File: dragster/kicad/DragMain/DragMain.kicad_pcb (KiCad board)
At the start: 2 copper layers, 56 x 100 mm, 23 parts, among them J1 Aux, J2 Servo 1, J3 Battery, J4 Motor L, J5 Motor R, J6 Sensors, J7 Motor L2, J8 Motor R2, U1 DFROBOT_HR8833, U2 TTGO_ESP32_TDisplay

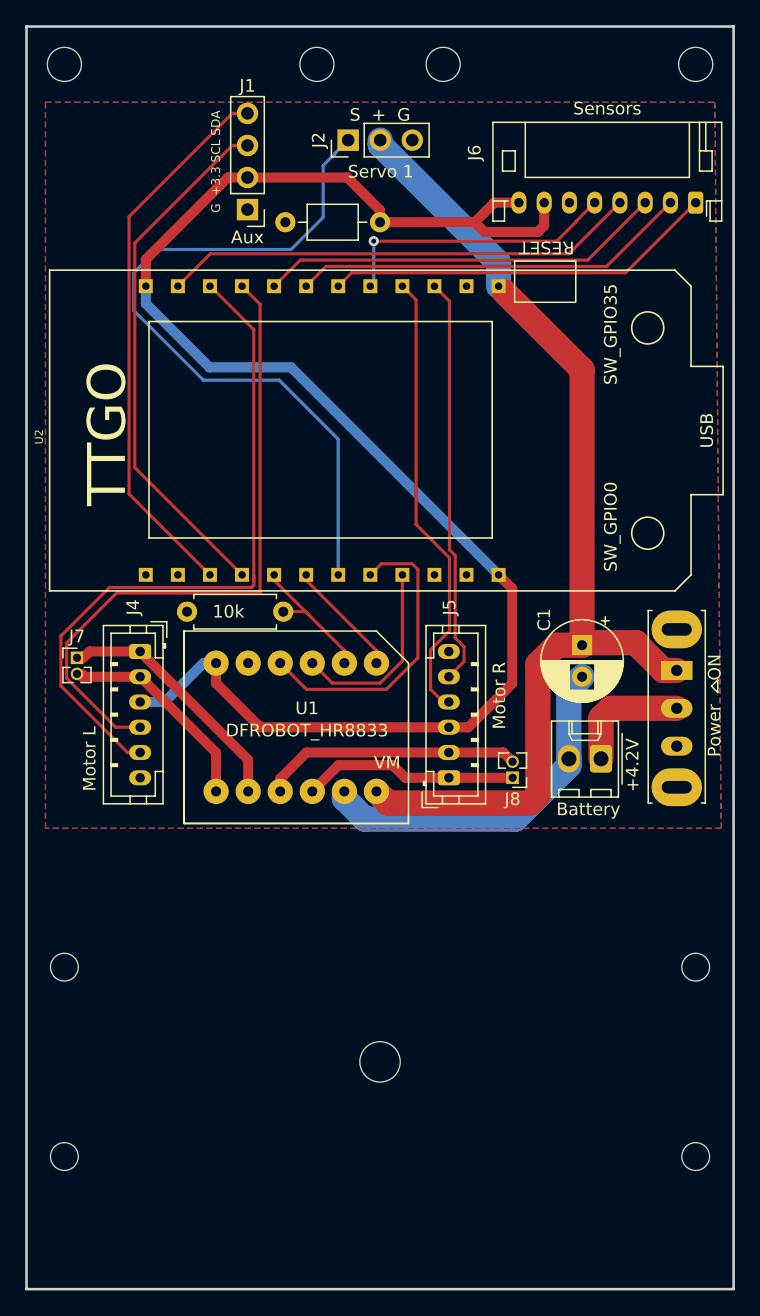
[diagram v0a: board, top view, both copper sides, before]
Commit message: Minor teaks to fix hole sizes and some positions
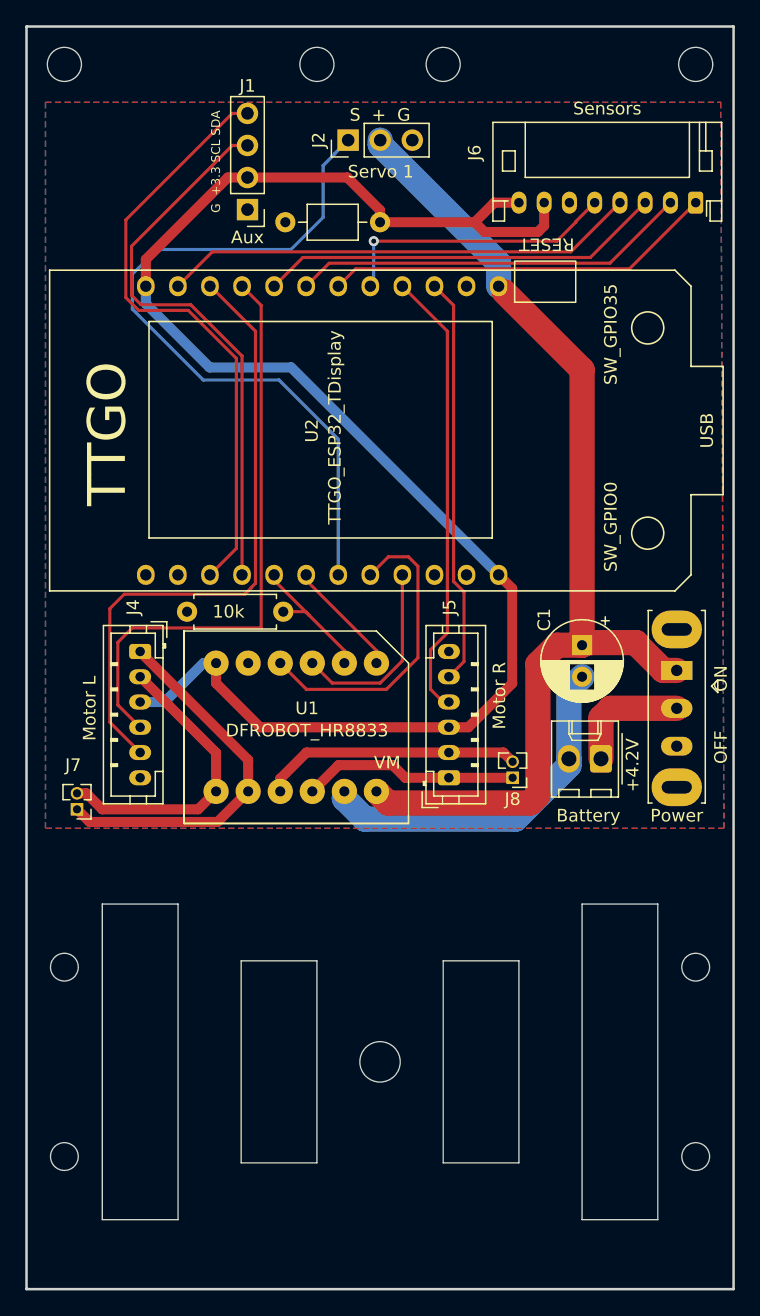
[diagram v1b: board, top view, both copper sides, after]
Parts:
- moved J7 12.0 mm to (91.0, 118.0), turned to 180 degrees
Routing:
- net Net-(U1-Pad8): track 19.3 -> 29.6 mm
- net Net-(U1-Pad7): track 16.4 -> 23.7 mm
- net GPIO38: track 52.1 -> 47.0 mm
- net GPIO37: track 55.0 -> 49.9 mm
- net GPIO21: track 43.8 -> 48.0 mm
- net GPIO22: track 41.9 -> 44.4 mm
- net GPIO13: track 24.1 -> 24.7 mm
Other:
- outline, holes or cut-outs redrawn
